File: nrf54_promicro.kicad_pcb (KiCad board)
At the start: 4 copper layers, 18 x 35 mm, 60 parts, among them J1 GSB1C4621DS1HR, J2 Conn_01x13_Socket, J3 Conn_01x13_Socket, U1 BQ24075RGT, U2 nRF54L1X, U3 TPS62172DSG, U4 AP22913CN4, Y1 32.768k, Y2 32M

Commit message: Continued to improve layout. Updated README.md
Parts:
- moved C23 0.06 mm to (142.9, 88.9)
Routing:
- net /P1.09: track 9.21 -> 8.28 mm
- net GND: track 51.2 -> 50.5 mm, vias 100 -> 101

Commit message: Improved Layout. Improved Silk/Fab.
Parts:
- moved C25 0.70 mm to (136.5, 81.6)
- moved R10 0.70 mm to (136.5, 80.9)
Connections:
- D1 pad 1: /~{CHG_STAT} -> GND
- U1 pad 9: /~{CHG_STAT} -> GND
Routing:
- net GND: track 50.5 -> 60.6 mm, vias 101 -> 77
- net /~{CHG_STAT}: track 7.28 -> 0.00 mm, vias 2 -> 0
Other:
- board text added: "0"
- board text added: "0 mm"
- board text added: "0.01 mm"
- board text added: "0.0152 mm"
- board text added: "0.02"
- board text added: "0.035 mm"
- board text added: "0.0764 mm"
- board text added: "0.10 mm / 0.09 mm"
- board text added: "0.200 mm"
- board text added: "0.865 mm"
- board text added: "1"
- board text added: "1.20 mm"
- board text added: "1080"
- board text added: "18.00 mm x 35.00 mm"
- board text added: "3.3"
- board text added: "3.7"
- board text added: "3V3"
- board text added: "4"
- board text added: "4.5"
- board text added: "7628"
- board text added: "B"
- board text added: "B.Cu"
- board text added: "B.Mask"
- board text added: "B.Paste"
- board text added: "B.Silkscreen"
- board text added: "BOARD CHARACTERISTICS"
- board text added: "Board Thickness:"
- board text added: "Board overall dimensions:"
- board text added: "Bottom Silk Screen"
- board text added: "Bottom Solder Mask"
- board text added: "Bottom Solder Paste"
- board text added: "Castellated pads:"
- board text added: "Color"
- board text added: "Copper Finish:"
- board text added: "Copper Layer Count:"
- board text added: "Dielectric"
- board text added: "Edge card connectors:"
- board text added: "Epsilon R"
- board text added: "F.Cu"
- board text added: "F.Mask"
- board text added: "F.Paste"
- board text added: "F.Silkscreen"
- board text added: "FR4"
- board text added: "GND"
- board text added: "Green"
- board text added: "Impedance Control:"
- board text added: "In1.Cu"
- board text added: "In2.Cu"
- board text added: "Layer Name"
- board text added: "Loss Tangent"
- board text added: "Material"
- board text added: "Min hole diameter:"
- board text added: "Min track/spacing:"
- board text added: "No"
- board text added: "None"
- board text added: "Not specified"
- board text added: "Plated Board Edge:"
- board text added: "RST"
- board text added: "SCK"
- board text added: "SWD"
- board text added: "Thickness (mm)"
- board text added: "Top Silk Screen"
- board text added: "Top Solder Mask"
- board text added: "Top Solder Paste"
- board text added: "Type"
- board text added: "Yes"
- board text added: "copper"
- board text added: "core"
- board text added: "prepreg"

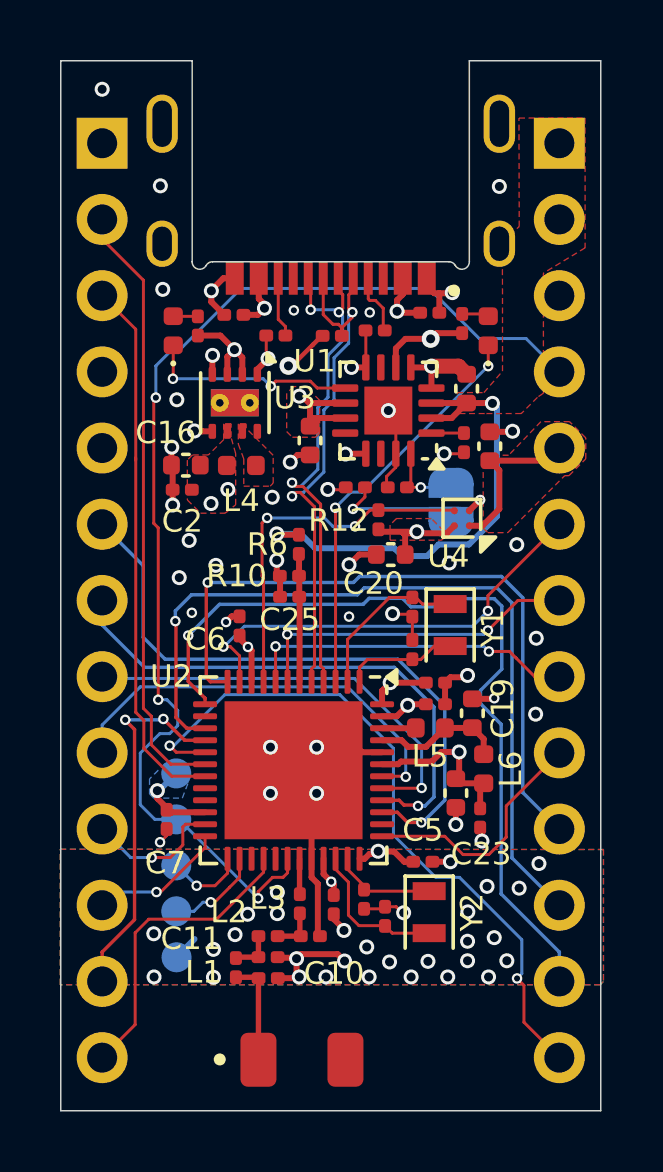
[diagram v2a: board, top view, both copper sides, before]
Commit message: Swapped U4 for lower Iq load switch. Fixed DRCs. Fixed Layout.
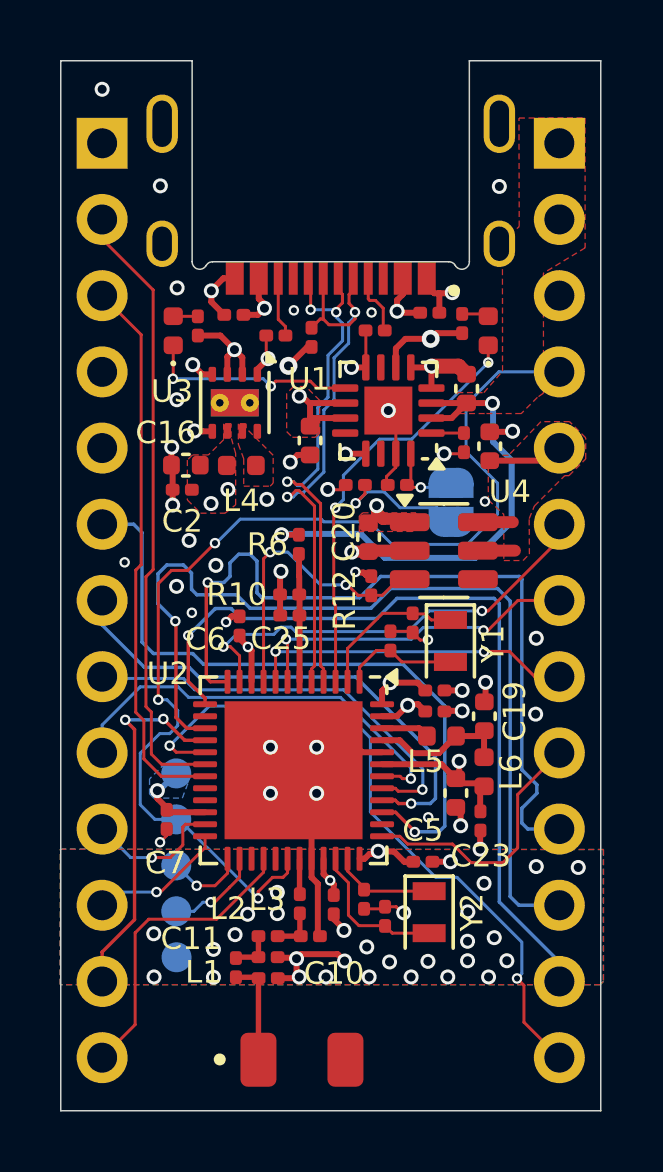
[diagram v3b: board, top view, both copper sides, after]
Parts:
- U2: value nRF54L1X -> nRF54L10
- U4: value AP22913CN4 -> TPS22917DBV; footprint Package_CSP:WLCSP-4-X1-WLB0909-4_0.89x0.89mm_P0.5mm -> Package_TO_SOT_SMD:SOT-23-6
- moved R12 2.21 mm to (139.2, 81.2), turned to -90 degrees
- moved U4 1.24 mm to (141.7, 80.0), turned to 0 degrees
- moved C20 0.94 mm to (139.2, 79.6), turned to -90 degrees
- moved C14 0.79 mm to (139.9, 83.0)
- moved R1 0.69 mm to (137.3, 72.9), turned to 90 degrees
- moved C25 0.62 mm to (136.5, 82.2)
- moved R10 0.62 mm to (136.5, 81.5)
- moved C13 0.53 mm to (140.6, 82.4)
- moved Y1 0.53 mm to (141.9, 83.0)
- moved L5 0.46 mm to (141.6, 86.2)
- moved C19 0.41 mm to (143.0, 85.5)
- moved C3 0.26 mm to (141.4, 84.7)
- moved C4 0.24 mm to (141.4, 85.4)
- moved C23 0.10 mm to (142.9, 89.0)
- moved L6 0.10 mm to (143.0, 87.4)
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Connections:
- D1 pad 1: GND -> /~{CHG_STAT}
- R12 pad 2: /EXT_EN -> /VEXT_DIS_L
- U1 pad 9: GND -> /~{CHG_STAT}
- U2 pad 9: /EXT_EN -> /VEXT_DIS_L
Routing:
- net /EXT_EN: track 12.2 -> 0.00 mm, vias 2 -> 0
- net /VEXT_DIS_L: track 0.00 -> 9.88 mm, vias 0 -> 2
- net GND: track 60.6 -> 52.9 mm, vias 77 -> 75
- net /~{CHG_STAT}: track 0.00 -> 7.13 mm, vias 0 -> 2
- net /P2.04_SPI_SDI: track 27.2 -> 31.0 mm
- net /P2.01_SPI_SCK: track 23.1 -> 26.5 mm
- net /RESETB: track 38.7 -> 36.3 mm
- net /P1.11_I2CSDA_AIN4: track 21.0 -> 22.5 mm
- net /P1.12_I2CSCL_AIN5: track 17.9 -> 17.0 mm
- net /USB_D_N: track 18.2 -> 19.0 mm
- net /P1.09: track 8.18 -> 8.83 mm
- net /P2.06: track 23.4 -> 22.8 mm
- net VEXT: track 5.47 -> 4.89 mm
- net VSYS: track 22.1 -> 21.5 mm, vias 4 -> 5
- net /P2.02_SPI_SDO: track 27.7 -> 27.2 mm
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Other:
- board text added: "Designs"

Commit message: Updated REAMDME.md. Moved lib files. Generated some output documentation.
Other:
- board text added: "0.20 mm"
- board text added: "02-24-2025"
- board text added: "DATE"
- board text added: "Initial Release"
- board text added: "NOTE"
- board text added: "Proto"
- board text added: "VERSION"
- board text removed: "0.200 mm"
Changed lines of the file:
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@@
 			(layer "F.Fab")
 		)
-		(fp_text user "PCB EDGE"
-			(at 0 5.2 0)
-			(layer "F.Fab")
-			(effects
-				(font
-					(size 0.8 0.8)
-					(thickness 0.15)
-				)
-			)
-		)
 		(pad "A1_B12" smd rect
 			(at -3.2 -5.15 180)
@@
 		)
 	)
-	(gr_text "0.200 mm"
+	(gr_text "0.20 mm"
 		(at 249.297138 66.913 0)
 		(layer "F.Fab")
@@
 		)
 	)
+	(gr_text "VERSION"
+		(at 264.96 18.27 0)
+		(layer "F.Fab")
+		(effects
+			(font
+				(size 1.5 1.5)
+				(thickness 0.3)
+				(bold yes)
+			)
+			(justify left bottom)
+		)
+	)
 	(gr_text "F.Paste"
 		(at 157.352857 93.394 0)
@@
 		)
 	)
+	(gr_text "DATE"
+		(at 220.06 18.14 0)
+		(layer "F.Fab")
+		(effects
+			(font
+				(size 1.5 1.5)
+				(thickness 0.3)
+				(bold yes)
+			)
+			(justify left bottom)
+		)
+	)
 	(gr_text "1"
 		(at 250.838573 129.454 0)
@@
 		)
 	)
+	(gr_text "Proto"
+		(at 265.56 23.23 0)
+		(layer "F.Fab")
+		(effects
+			(font
+				(size 1.5 1.5)
+				(thickness 0.1875)
+			)
+			(justify left bottom)
+		)
+	)
 	(gr_text "0"
 		(at 263.724288 115.03 0)
@@
 		)
 	)
+	(gr_text "Initial Release"
+		(at 237.55 23.63 0)
+		(layer "F.Fab")
+		(effects
+			(font
+				(size 1.5 1.5)
+				(thickness 0.1875)
+			)
+			(justify left bottom)
+		)
+	)
 	(gr_text "0.0152 mm"
 		(at 214.31 115.03 0)
@@
 		)
 	)
+	(gr_text "NOTE"
+		(at 242.91 18.07 0)
+		(layer "F.Fab")
+		(effects
+			(font
+				(size 1.5 1.5)
+				(thickness 0.3)
+				(bold yes)
+			)
+			(justify left bottom)
+		)
+	)
 	(gr_text "Impedance Control: "
 		(at 224.354281 70.87 0)
@@
 		)
 	)
+	(gr_text "02-24-2025"
+		(at 215.03 23.5 0)
+		(layer "F.Fab")
+		(effects
+			(font
+				(size 1.5 1.5)
+				(thickness 0.1875)
+			)
+			(justify left bottom)
+		)
+	)
 	(gr_text "0"
 		(at 263.724288 133.06 0)
@@
 	)
 	(table
-		(column_count 2)
+		(column_count 3)
 		(layer "F.Fab")
 		(border
@@
 			(header yes)
 			(stroke
-				(width 0.1)
+				(width 0.2)
 				(type solid)
 			)
@@
 			(cols yes)
 			(stroke
-				(width 0.1)
+				(width 0.2)
 				(type solid)
 			)
 		)
-		(column_widths 20.59 20.59)
-		(row_heights 3.15 3.15 3.15 3.15 3.15)
+		(column_widths 24.77 24.77 24.77)
+		(row_heights 4.97 4.97 4.97 4.97)
 		(cells
-			(table_cell "DATE"
-				(start 241.88 13.72)
-				(end 262.47 16.87)
+			(table_cell ""
+				(start 208.95 14.77)
+				(end 233.72 19.74)
 				(margins 1.0025 1.0025 1.0025 1.0025)
 				(span 1 1)
@@
 					(font
 						(size 1.27 1.27)
-						(thickness 0.254)
-						(bold yes)
 					)
 					(justify left top)
 				)
 			)
-			(table_cell "COMMENT"
-				(start 262.47 13.72)
-				(end 283.06 16.87)
+			(table_cell ""
+				(start 233.72 14.77)
+				(end 258.49 19.74)
 				(margins 1.0025 1.0025 1.0025 1.0025)
 				(span 1 1)
@@
 					(font
 						(size 1.27 1.27)
-						(thickness 0.254)
-						(bold yes)
 					)
 					(justify left top)
 				)
 			)
-			(table_cell "02-24-2025"
-				(start 241.88 16.87)
-				(end 262.47 20.02)
+			(table_cell ""
+				(start 258.49 14.77)
+				(end 283.26 19.74)
 				(margins 1.0025 1.0025 1.0025 1.0025)
 				(span 1 1)
@@
 				)
 			)
-			(table_cell "Initial Release"
-				(start 262.47 16.87)
-				(end 283.06 20.02)
+			(table_cell ""
+				(start 208.95 19.74)
+				(end 233.72 24.71)
 				(margins 1.0025 1.0025 1.0025 1.0025)
 				(span 1 1)
@@
 			)
 			(table_cell ""
-				(start 241.88 20.02)
-				(end 262.47 23.17)
+				(start 233.72 19.74)
+				(end 258.49 24.71)
 				(margins 1.0025 1.0025 1.0025 1.0025)
 				(span 1 1)
@@
 			)
 			(table_cell ""
-				(start 262.47 20.02)
-				(end 283.06 23.17)
+				(start 258.49 19.74)
+				(end 283.26 24.71)
 				(margins 1.0025 1.0025 1.0025 1.0025)
 				(span 1 1)
@@
 			)
 			(table_cell ""
-				(start 241.88 23.17)
-				(end 262.47 26.32)
+				(start 208.95 24.71)
+				(end 233.72 29.68)
 				(margins 1.0025 1.0025 1.0025 1.0025)
 				(span 1 1)
@@
 			)
 			(table_cell ""
-				(start 262.47 23.17)
-				(end 283.06 26.32)
+				(start 233.72 24.71)
+				(end 258.49 29.68)
 				(margins 1.0025 1.0025 1.0025 1.0025)
 				(span 1 1)
@@
 			)
 			(table_cell ""
-				(start 241.88 26.32)
-				(end 262.47 29.47)
+				(start 258.49 24.71)
+				(end 283.26 29.68)
 				(margins 1.0025 1.0025 1.0025 1.0025)
 				(span 1 1)
@@
 			)
 			(table_cell ""
-				(start 262.47 26.32)
-				(end 283.06 29.47)
+				(start 208.95 29.68)
+				(end 233.72 34.65)
+				(margins 1.0025 1.0025 1.0025 1.0025)
+				(span 1 1)
+				(layer "F.Fab")
+				(effects
+					(font
+						(size 1.27 1.27)
+					)
+					(justify left top)
+				)
+			)
+			(table_cell ""
+				(start 233.72 29.68)
+				(end 258.49 34.65)
+				(margins 1.0025 1.0025 1.0025 1.0025)
+				(span 1 1)
+				(layer "F.Fab")
+				(effects
+					(font
+						(size 1.27 1.27)
+					)
+					(justify left top)
+				)
+			)
+			(table_cell ""
+				(start 258.49 29.68)
+				(end 283.26 34.65)
 				(margins 1.0025 1.0025 1.0025 1.0025)
 				(span 1 1)
@@
 	)
 	(zone
-		(net 5)
-		(net_name "/BLE_PCB_ANT")
-		(layer "F.Cu")
-		(name "$teardrop_padvia$")
-		(hatch full 0.1)
-		(priority 30000)
-		(attr
-			(teardrop
-				(type padvia)
-			)
-		)
-		(connect_pads yes
-			(clearance 0)
-		)
-		(min_thickness 0.0254)
-		(filled_areas_thickness no)
-		(fill yes
-			(thermal_gap 0.5)
-			(thermal_bridge_width 0.5)
-			(island_removal_mode 1)
-			(island_area_min 10)
-		)
-		(polygon
-			(pts
-				(xy 135.58 95.5) (xy 135.4 95.5) (xy 134.90903 96.254329) (xy 135.49 97.001) (xy 136.07097 96.254329)
-			)
-		)
-	)
-	(zone
 		(net 3)
 		(net_name "3V3_VCC")
@@
 			)
 		)
+	)
+	(zone
+		(net 5)
+		(net_name "/BLE_PCB_ANT")
+		(layer "F.Cu")
+		(name "$teardrop_padvia$")
+		(hatch full 0.1)
+		(priority 30000)
+		(attr
+			(teardrop
+				(type padvia)
+			)
+		)
+		(connect_pads yes
+			(clearance 0)
+		)
+		(min_thickness 0.0254)
+		(filled_areas_thickness no)
+		(fill yes
+			(thermal_gap 0.5)
+			(thermal_bridge_width 0.5)
+			(island_removal_mode 1)
+			(island_area_min 10)
+		)
+		(polygon
+			(pts
+				(xy 135.58 95.5) (xy 135.4 95.5) (xy 134.90903 96.254329) (xy 135.49 97.001) (xy 136.07097 96.254329)
+			)
+		)

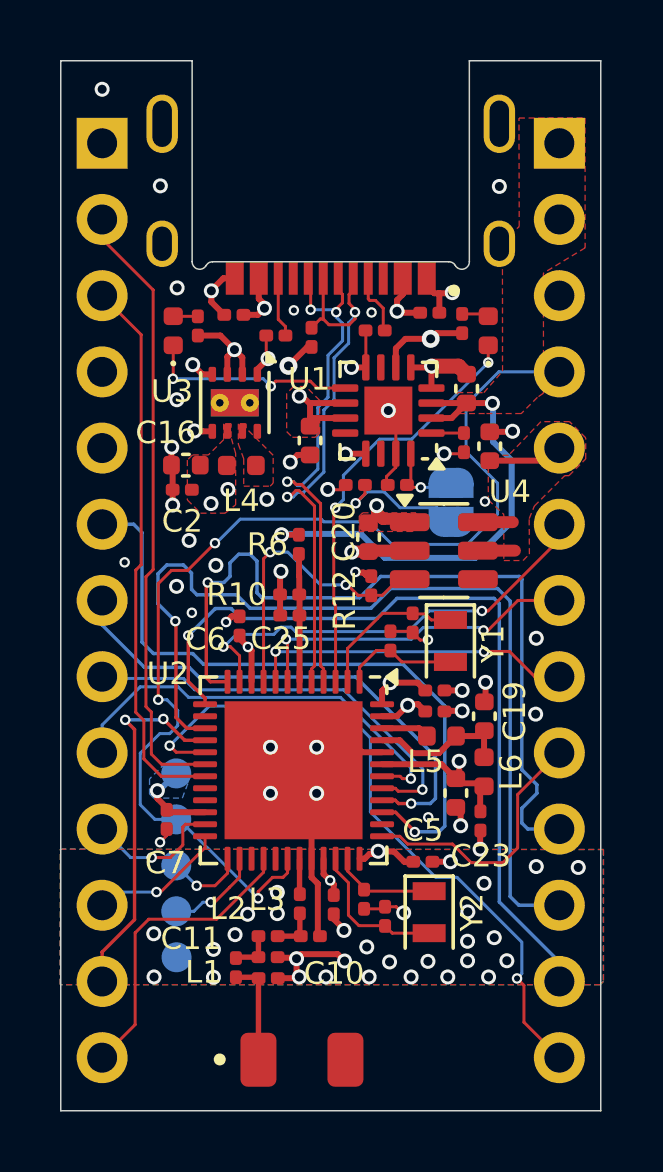
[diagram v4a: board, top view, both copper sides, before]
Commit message: BOM updates, schematic and layout updated due to BOM updated
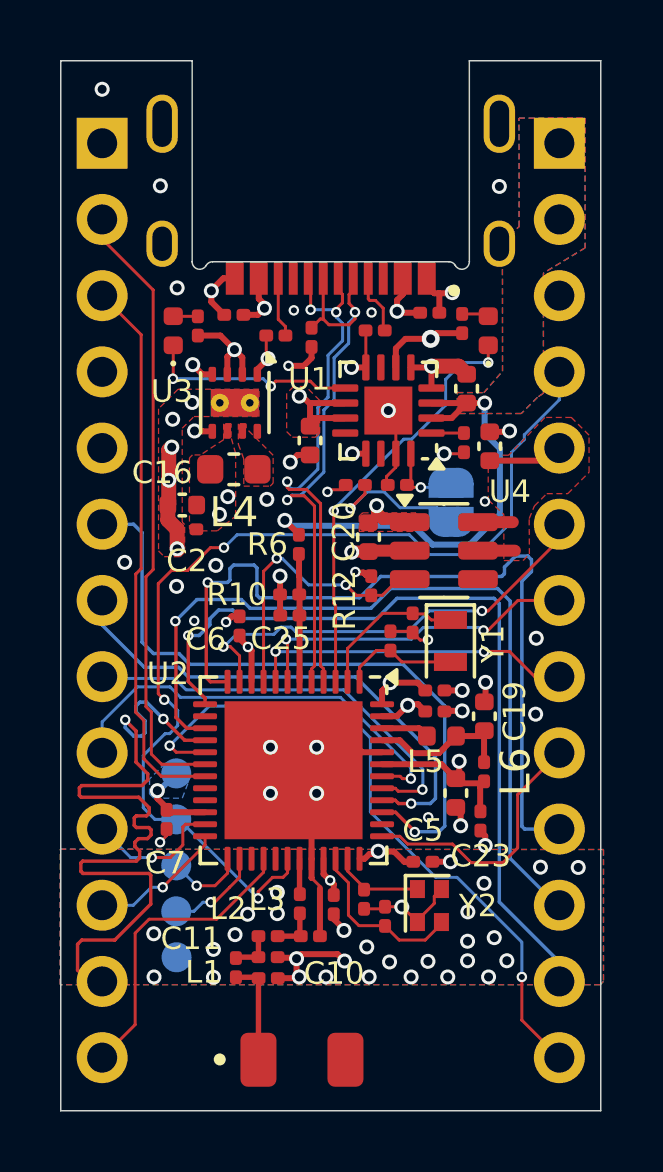
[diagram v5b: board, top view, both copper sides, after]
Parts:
- C13, C14: value 12P -> 9P
- C17, C18: value 12P -> 8P
- L4: footprint Inductor_SMD:L_0402_1005Metric -> Inductor_SMD:L_0603_1608Metric
- L6: value L -> 120R @ 100MHz; footprint Inductor_SMD:L_0402_1005Metric -> Inductor_SMD:L_0201_0603Metric
- U2: value nRF54L10 -> nRF54L15
- Y2: footprint Crystal:Crystal_SMD_2012-2Pin_2.0x1.2mm -> Oscillator:Oscillator_SMD_Abracon_ASCO-4Pin_1.6x1.2mm
- moved C16 1.34 mm to (132.9, 78.5)
- moved C2 1.33 mm to (133.1, 79.3)
- moved L4 0.28 mm to (134.7, 77.3)
- moved Y2 0.22 mm to (141.2, 91.9), turned to 0 degrees
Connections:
- Y2 pad 2: /XC1 -> GND
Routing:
- net /P2.05_SPI_CS_L: track 12.3 -> 25.9 mm
- net GND: track 52.9 -> 62.3 mm, vias 75 -> 76
- net /P2.04_SPI_SDI: track 31.0 -> 27.2 mm
- net /RESETB: track 36.3 -> 34.2 mm
- net VBAT: track 16.7 -> 15.7 mm
- net /XC1: track 5.00 -> 5.77 mm
- net /P2.01_SPI_SCK: track 26.5 -> 27.3 mm
- added copper zone on B.Cu, net VBAT
